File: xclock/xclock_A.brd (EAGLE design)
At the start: 50 x 50 mm, 27 parts, among them J1 PINHD-3X7/90, U1 5P49V5923, U2 SI7021, X1 9C-24.000MEEJ-T

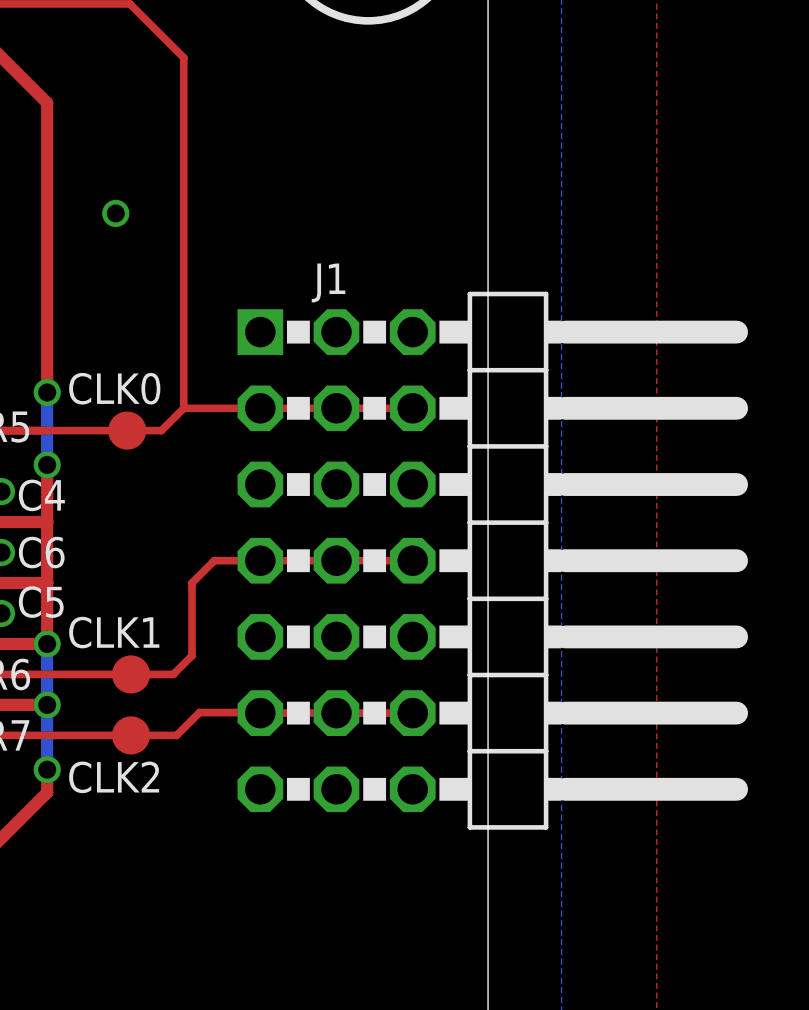
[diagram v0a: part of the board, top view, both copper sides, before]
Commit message: xclock: new pinhead 3x7 symbol
Signed-off-by: malo <pavol.malosek@gmail.com>
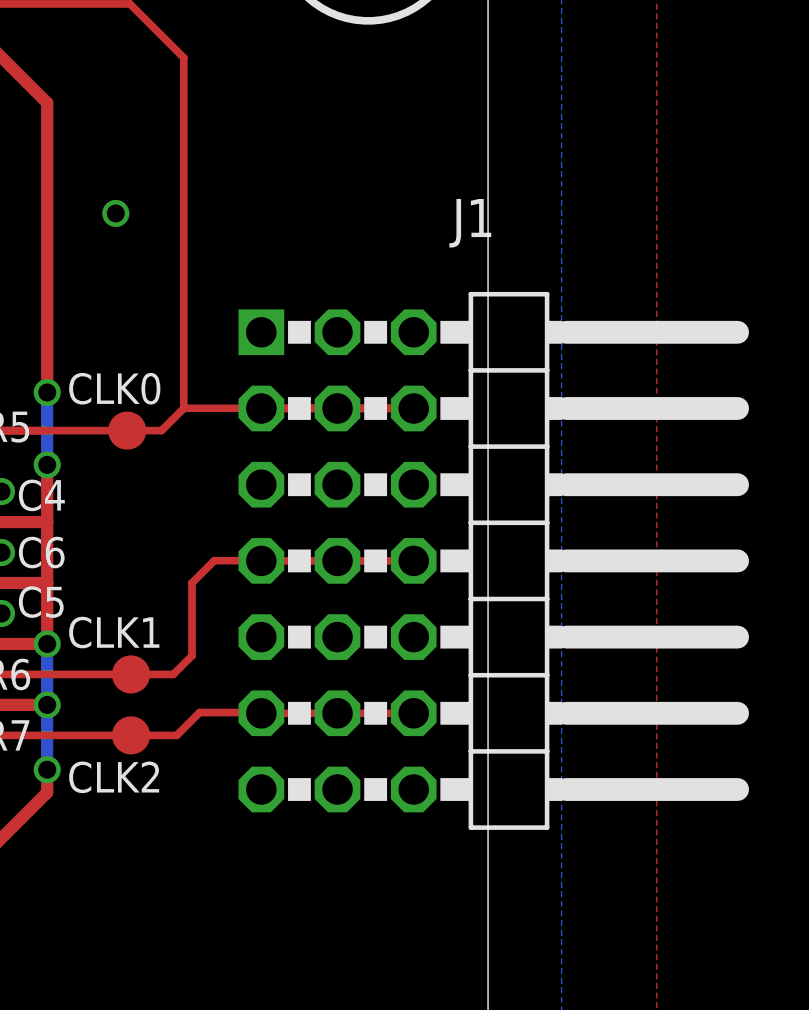
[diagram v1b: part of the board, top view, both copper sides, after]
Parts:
- J1: device pinhead:3X07/90 -> 25pinhead:3X07/90
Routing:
- net OUT0: track 90.0 -> 94.0 mm
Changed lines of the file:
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@@
 </element>
 <element name="PWR1" library="25cmsquare" package="LIWE_12_PIN" value="" x="25" y="25" smashed="yes" rot="R180"/>
-<element name="J1" library="pinhead" package="3X07/90" value="PINHD-3X7/90" x="51.3" y="25" smashed="yes" rot="R270">
-<attribute name="NAME" x="44.188" y="33.89" size="1.016" layer="25" font="vector" ratio="15"/>
-</element>
 <element name="U2" library="25cmsquare" package="SI7021" value="SI7021" x="25.146" y="38.354" smashed="yes">
 <attribute name="NAME" x="23.658" y="39.999" size="1.016" layer="21" font="vector" ratio="15"/>
@@
 <attribute name="NAME" x="23.5754" y="7.608" size="1.016" layer="25" font="vector" ratio="15"/>
 </element>
+<element name="J1" library="25pinhead" package="3X07/90" value="PINHD-3X7/90" x="51.3334" y="24.9936" rot="R270"/>
 </elements>
 <signals>
@@
 <contactref element="PWR1" pad="3"/>
 <contactref element="PWR1" pad="8"/>
-<contactref element="J1" pad="1"/>
-<contactref element="J1" pad="7"/>
-<contactref element="J1" pad="13"/>
-<contactref element="J1" pad="19"/>
-<contactref element="J1" pad="2"/>
-<contactref element="J1" pad="8"/>
-<contactref element="J1" pad="14"/>
-<contactref element="J1" pad="20"/>
-<contactref element="J1" pad="3"/>
-<contactref element="J1" pad="21"/>
-<contactref element="J1" pad="15"/>
-<contactref element="J1" pad="9"/>
 <via x="17.018" y="37.338" extent="1-16" drill="0.6" shape="square"/>
 <via x="33.02" y="37.338" extent="1-16" drill="0.6" shape="square"/>
@@
 <via x="22.2758" y="38.3794" extent="1-16" drill="0.6" shape="square"/>
 <contactref element="GND" pad="1"/>
+<contactref element="J1" pad="3"/>
+<contactref element="J1" pad="9"/>
+<contactref element="J1" pad="15"/>
+<contactref element="J1" pad="21"/>
+<contactref element="J1" pad="1"/>
+<contactref element="J1" pad="2"/>
+<contactref element="J1" pad="7"/>
+<contactref element="J1" pad="8"/>
+<contactref element="J1" pad="13"/>
+<contactref element="J1" pad="14"/>
+<contactref element="J1" pad="19"/>
+<contactref element="J1" pad="20"/>
 </signal>
 <signal name="XOUT">
@@
 <contactref element="CLK0" pad="TP"/>
 <contactref element="PWR1" pad="5"/>
-<contactref element="J1" pad="4"/>
-<contactref element="J1" pad="5"/>
-<contactref element="J1" pad="6"/>
-<wire x1="42.41" y1="30.08" x2="39.859" y2="30.08" width="0.254" layer="1"/>
 <wire x1="39.859" y1="30.08" x2="39.116" y2="29.337" width="0.254" layer="1"/>
 <wire x1="37.973" y1="29.337" x2="32.473" y2="29.337" width="0.254" layer="1"/>
-<wire x1="42.41" y1="30.08" x2="44.95" y2="30.08" width="0.254" layer="1"/>
-<wire x1="44.95" y1="30.08" x2="47.49" y2="30.08" width="0.254" layer="1"/>
 <wire x1="32.473" y1="29.337" x2="35.306" y2="29.337" width="0.254" layer="1"/>
 <wire x1="38.062" y1="43.561" x2="7.874" y2="43.561" width="0.254" layer="1"/>
@@
 <wire x1="6.096" y1="20.955" x2="5.061" y2="19.92" width="0.254" layer="1"/>
 <wire x1="5.061" y1="19.92" x2="2.5" y2="19.92" width="0.254" layer="1"/>
+<contactref element="J1" pad="6"/>
+<contactref element="J1" pad="4"/>
+<contactref element="J1" pad="5"/>
+<wire x1="39.859" y1="30.08" x2="44.4246" y2="30.08" width="0.254" layer="1"/>
+<wire x1="44.4246" y1="30.08" x2="46.9392" y2="30.08" width="0.254" layer="1"/>
+<wire x1="46.9392" y1="30.08" x2="47.5234" y2="30.08" width="0.254" layer="1"/>
+<wire x1="47.5234" y1="30.08" x2="47.5234" y2="30.0736" width="0.254" layer="1"/>
+<wire x1="42.4434" y1="30.0736" x2="44.4246" y2="30.0736" width="0.254" layer="1"/>
+<wire x1="44.4246" y1="30.0736" x2="44.4246" y2="30.08" width="0.254" layer="1"/>
+<wire x1="44.9834" y1="30.0736" x2="46.9392" y2="30.0736" width="0.254" layer="1"/>
+<wire x1="46.9392" y1="30.0736" x2="46.9392" y2="30.08" width="0.254" layer="1"/>
 </signal>
 <signal name="OUT1">
 <contactref element="CLK1" pad="TP"/>
 <contactref element="R6" pad="1"/>
-<contactref element="J1" pad="10"/>
-<contactref element="J1" pad="11"/>
-<contactref element="J1" pad="12"/>
 <wire x1="32.473" y1="21.209" x2="38.1" y2="21.209" width="0.254" layer="1"/>
 <wire x1="39.508" y1="21.209" x2="40.132" y2="21.833" width="0.254" layer="1"/>
 <wire x1="40.132" y1="21.833" x2="40.132" y2="24.257" width="0.254" layer="1"/>
 <wire x1="40.132" y1="24.257" x2="40.875" y2="25" width="0.254" layer="1"/>
-<wire x1="40.875" y1="25" x2="42.41" y2="25" width="0.254" layer="1"/>
-<wire x1="42.41" y1="25" x2="44.95" y2="25" width="0.254" layer="1"/>
-<wire x1="44.95" y1="25" x2="47.49" y2="25" width="0.254" layer="1"/>
 <wire x1="39.508" y1="21.209" x2="38.1" y2="21.209" width="0.254" layer="1"/>
+<contactref element="J1" pad="12"/>
+<contactref element="J1" pad="10"/>
+<contactref element="J1" pad="11"/>
+<wire x1="40.875" y1="25" x2="42.4434" y2="25" width="0.254" layer="1"/>
+<wire x1="42.4434" y1="25" x2="42.4434" y2="24.9936" width="0.254" layer="1"/>
+<wire x1="42.4434" y1="24.9936" x2="44.9834" y2="24.9936" width="0.254" layer="1"/>
+<wire x1="44.9834" y1="24.9936" x2="47.5234" y2="24.9936" width="0.254" layer="1"/>
 </signal>
 <signal name="OUT2">
 <contactref element="R7" pad="1"/>
 <contactref element="CLK2" pad="TP"/>
-<contactref element="J1" pad="16"/>
-<contactref element="J1" pad="17"/>
-<contactref element="J1" pad="18"/>
 <wire x1="32.473" y1="19.177" x2="38.1" y2="19.177" width="0.254" layer="1"/>
 <wire x1="39.624" y1="19.177" x2="40.386" y2="19.939" width="0.254" layer="1"/>
 <wire x1="40.386" y1="19.939" x2="42.429" y2="19.939" width="0.254" layer="1"/>
-<wire x1="42.429" y1="19.939" x2="42.41" y2="19.92" width="0.254" layer="1"/>
-<wire x1="42.41" y1="19.92" x2="44.95" y2="19.92" width="0.254" layer="1"/>
-<wire x1="44.95" y1="19.92" x2="47.49" y2="19.92" width="0.254" layer="1"/>
 <wire x1="39.624" y1="19.177" x2="38.1" y2="19.177" width="0.254" layer="1"/>
+<contactref element="J1" pad="18"/>
+<contactref element="J1" pad="16"/>
+<contactref element="J1" pad="17"/>
+<wire x1="47.5234" y1="19.9136" x2="44.9834" y2="19.9136" width="0.254" layer="1"/>
+<wire x1="44.9834" y1="19.9136" x2="42.4434" y2="19.9136" width="0.254" layer="1"/>
+<wire x1="42.429" y1="19.939" x2="42.4434" y2="19.9136" width="0" layer="19" extent="1-1"/>
 </signal>
 <signal name="VDDD">
